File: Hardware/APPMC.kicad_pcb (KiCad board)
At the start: 2 copper layers, 85 x 50 mm, 117 parts, among them J1 + 30V max, J10 STLINK-V3, J101 ADC_C, J102 ADC_D, J11 Waveshare 14747, J12 Conn_01x04, J13 Micro-USB B, J14 VDD, J15 PWM, J16 ADC_B, J17 3.0V, J18 1.5V, J19 DAC_A, J2 VOut, J20 ADC_A, J21 DAC_B, J22 Jumper-2B-Open, J23 GND, J24 Jumper-2B-Open, J3 Jumper-2B-Open, J4 Jumper-2B-Open, J6 Conn_01x04, J7 VCC, J8 Conn_01x04, J9 Waveshare 18179, M4 Logo_Open_Hardware_Small, Q1 SI2343CDS-T1-GE3, Q2 ZXMP4A16GTA, Q3 ZXMP4A16GTA, Q4 BSS123, SW1 RESET, U1 INA823, U101 OPA320, U2 3.3V, U3 REF2030, U4 MAX12931, U5 STM32G0B1CEUx, U6 24CW640T-I/OT, U7 USBLC6-4SC6, U8 OPA378/387/392, U9 OPA378/387/392, Y1 32.768kHz

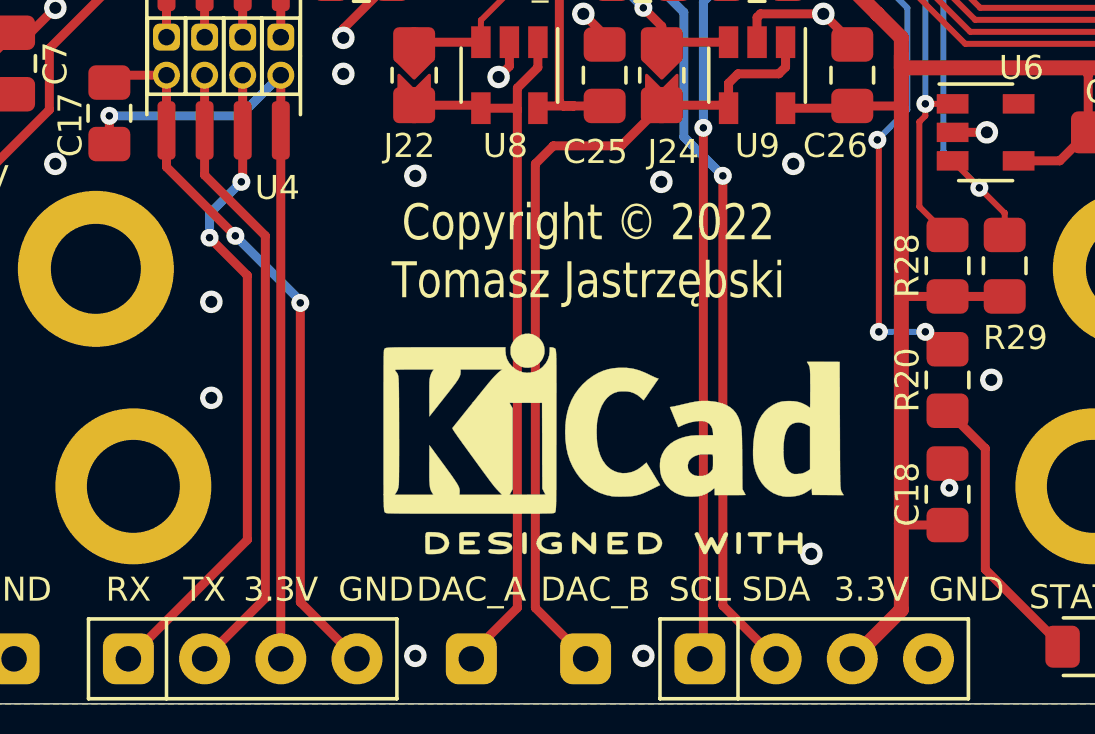
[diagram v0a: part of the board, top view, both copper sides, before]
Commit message: docs/license info update
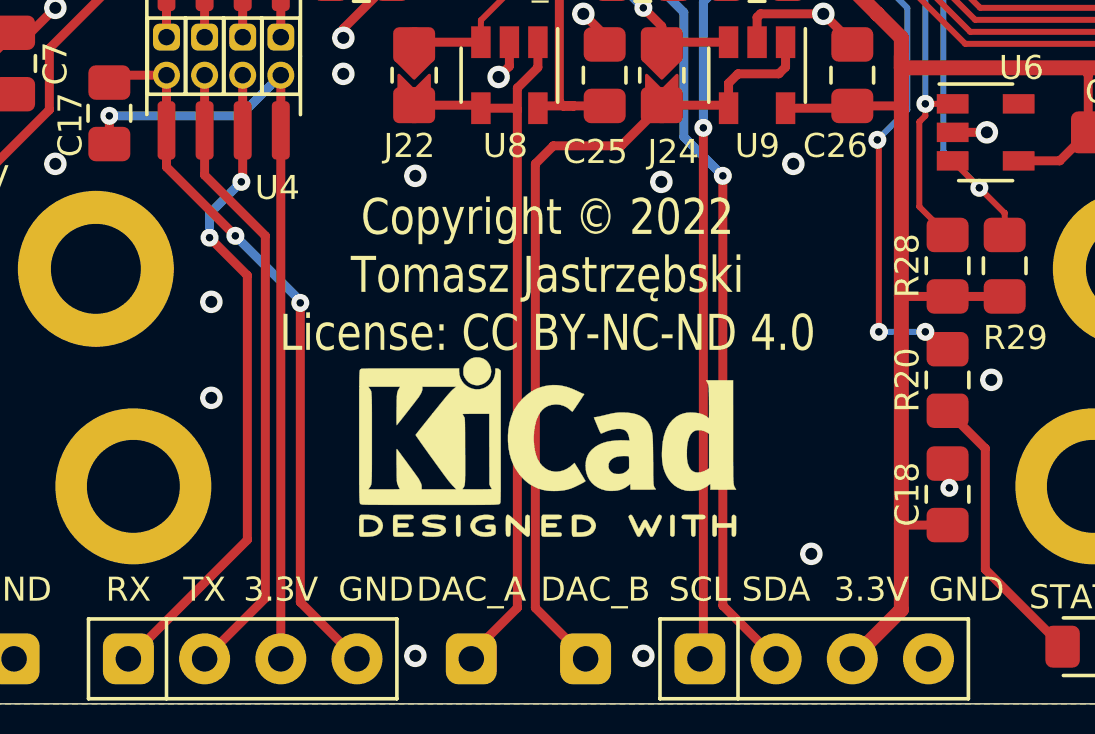
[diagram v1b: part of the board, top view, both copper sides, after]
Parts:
- M4: value Logo_Open_Hardware_Small -> KiCad-Logo2_5mm_SilkScreen; footprint Symbol:KiCad-Logo2_6mm_SilkScreen -> Symbol:KiCad-Logo2_5mm_SilkScreen
- moved M4 2.33 mm to (168.8, 131.4)
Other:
- board text added: "Copyright © 2022 Tomasz Jastrzębski License: CC BY-NC-ND 4.0"
- board text removed: "Copyright © 2022 Tomasz Jastrzębski"

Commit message: updates to 3.1
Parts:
- J12: value Conn_01x04 -> I2C
- J6: value Conn_01x04 -> STLINK-V2
- M4: value KiCad-Logo2_5mm_SilkScreen -> Logo_Open_Hardware_Small
- R9: value 3.44k -> 3.4k
- moved M4 0.37 mm to (168.8, 131.8)
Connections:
- U5 pad 28: /BTN -> (no net)
- U5 pad 44: (no net) -> /BTN
- U5 pad 49: GND -> (no net)
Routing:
- net /BTN: track 16.3 -> 19.2 mm
- net GND: vias 108 -> 110

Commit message: update
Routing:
- net GND: vias 110 -> 111

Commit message: 2022-09
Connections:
- net /~CS renamed /~{CS}
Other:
- net class Default removed
- board text added: "~{CS}"
- board text removed: "~CS"
